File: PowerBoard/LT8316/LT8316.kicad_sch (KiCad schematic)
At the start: 42 parts, among them J1 AuxConn, Q1 STD11N65M2, SW1 POWER_SW, T1 11328-T078, U2 LT8316EFE#PBF

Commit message: nearlyready
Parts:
- C15: MPN (none) -> C2918513
- C25: MPN C2761574 -> C240475
- C26: MPN (none) -> C240475
- J1: MPN C157991 -> C161870
- SW1: MPN (none) -> C144394
- T1: MPN (none) -> C7423050

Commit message: fixeddimensions
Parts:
- removed C25, C26: 2200uF 200V, Capacitor_THT:CP_Radial_D30.0mm_P10.00mm_SnapIn, symbol Device:C_Polarized
- removed H1, H2, H3, H4: BATT-Hole, MountingHole:MountingHole_3.2mm_M3, symbol Mechanical:MountingHole_Pad
- added C25 (x3), C26 (x3): 330u 200V, Capacitor_THT:CP_Radial_D18.0mm_P7.50mm, symbol Device:C_Polarized
- C12: value 47p 100V -> 47p; footprint Capacitor_SMD:C_0603_1608Metric -> Capacitor_SMD:C_0805_2012Metric; MPN C527044 -> C14857
- C8: footprint Capacitor_SMD:C_0805_2012Metric -> Capacitor_SMD:C_1206_3216Metric; MPN C784084 -> C113894
- R10: value 121k -> 120k; MPN C2933296 -> C17436
- R11: value 4.99k -> 6.2k; MPN C17677 -> C17767
- R12: value 44.2k -> 56k; MPN C2960780 -> C17756
- R3: value 499k -> 470k; footprint Resistor_SMD:R_1206_3216Metric -> Resistor_SMD:R_0805_2012Metric; MPN C102210 -> C17709
- R7: value 56.2k -> 56k; MPN C2930117 -> C17756
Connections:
- net +BATT: now also C25.1, C25.1, C25.1, C26.1, C26.1, C26.1
- net -BATT: now also C25.2, C25.2, C25.2, C26.2, C26.2, C26.2
- no-connect marks 4 -> 0
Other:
- note added: "EN Voltage divider has to provide voltage > 1.2V but cannot exeed 40V 470k and 20k gives operating range 30-300V+ giving 1.224V and 12.24V"
- note added: "For 100x220 enclosure"
- note added: "Power supply for 200V applications"
- note added: "Total Capacity 1980uF"
- note added: "transformer replacements Sumida 11328-T074 - 12V/3A Würth 750317463 - 12V/4A Würth 750317589 - 12V/3A"
- note removed: "EN Voltage divider has to provide voltage > 1.2V but cannot exeed 40V 499k and 20k gives operating range 32-300V+ giving 1.233V and 11.5V"
- note removed: "Total Capacity 4400uF"
- moved on the sheet: C10, C11, C12, C13, C14, C15, C16, C17, C7, C8, C9, D1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

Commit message: small changes for lt
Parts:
- C10: value 47p 25V -> 47p; footprint Capacitor_SMD:C_0805_2012Metric -> GigaVescLibs:C_0603_1608Metric_L; MPN C14857 -> C1671
- C12: footprint Capacitor_SMD:C_0805_2012Metric -> GigaVescLibs:C_0603_1608Metric_L; MPN C14857 -> C1671
- C14: footprint Capacitor_SMD:C_0805_2012Metric -> Capacitor_SMD:C_0603_1608Metric; MPN C28260 -> C1604
- C9: footprint Capacitor_SMD:C_0805_2012Metric -> GigaVescLibs:C_0603_1608Metric_L; MPN C28233 -> C14663
- R1: footprint Resistor_SMD:R_0805_2012Metric -> Resistor_SMD:R_0603_1608Metric; MPN C149504 -> C25803
- R10: footprint Resistor_SMD:R_0805_2012Metric -> Resistor_SMD:R_0603_1608Metric; MPN C17436 -> C25808
- R11: footprint Resistor_SMD:R_0805_2012Metric -> Resistor_SMD:R_0603_1608Metric; MPN C17767 -> C4260
- R12: footprint Resistor_SMD:R_0805_2012Metric -> Resistor_SMD:R_0603_1608Metric; MPN C17756 -> C23206
- R13: footprint Resistor_SMD:R_0805_2012Metric -> Resistor_SMD:R_0603_1608Metric; MPN C17544 -> C22950
- R14: footprint Resistor_SMD:R_0805_2012Metric -> Resistor_SMD:R_0603_1608Metric; MPN C17408 -> C22775
- R16, R4: footprint Resistor_SMD:R_0805_2012Metric -> Resistor_SMD:R_0603_1608Metric; MPN C4328 -> C4184
- R2: footprint Resistor_SMD:R_0805_2012Metric -> Resistor_SMD:R_0603_1608Metric; MPN C17398 -> C4177
- R3: footprint Resistor_SMD:R_0805_2012Metric -> Resistor_SMD:R_0603_1608Metric; MPN C17709 -> C23178
- R6: footprint Resistor_SMD:R_0805_2012Metric -> Resistor_SMD:R_0603_1608Metric; MPN C17414 -> C25804
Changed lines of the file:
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@@
       (effects (font (size 1.27 1.27)))
     )
-    (property "Footprint" "Resistor_SMD:R_0805_2012Metric" (at 68.58 128.778 90)
+    (property "Footprint" "Resistor_SMD:R_0603_1608Metric" (at 68.58 128.778 90)
       (effects (font (size 1.27 1.27)) hide)
     )
@@
       (effects (font (size 1.27 1.27)) hide)
     )
-    (property "MPN" "C4328" (at 68.58 127 90)
+    (property "MPN" "C4184" (at 68.58 127 90)
       (effects (font (size 1.27 1.27)) hide)
     )
@@
       (effects (font (size 1.27 1.27)))
     )
-    (property "Footprint" "Resistor_SMD:R_0805_2012Metric" (at 153.67 140.208 90)
+    (property "Footprint" "Resistor_SMD:R_0603_1608Metric" (at 153.67 140.208 90)
       (effects (font (size 1.27 1.27)) hide)
     )
@@
       (effects (font (size 1.27 1.27)) hide)
     )
-    (property "MPN" "C17544" (at 153.67 138.43 90)
+    (property "MPN" "C22950" (at 153.67 138.43 90)
       (effects (font (size 1.27 1.27)) hide)
     )
@@
       (effects (font (size 1.27 1.27)))
     )
-    (property "Footprint" "Resistor_SMD:R_0805_2012Metric" (at 67.31 103.378 90)
+    (property "Footprint" "Resistor_SMD:R_0603_1608Metric" (at 67.31 103.378 90)
       (effects (font (size 1.27 1.27)) hide)
     )
@@
       (effects (font (size 1.27 1.27)) hide)
     )
-    (property "MPN" "C4328" (at 67.31 101.6 90)
+    (property "MPN" "C4184" (at 67.31 101.6 90)
       (effects (font (size 1.27 1.27)) hide)
     )
@@
       (effects (font (size 1.27 1.27)) (justify left))
     )
-    (property "Footprint" "Resistor_SMD:R_0805_2012Metric" (at 139.192 129.54 90)
+    (property "Footprint" "Resistor_SMD:R_0603_1608Metric" (at 139.192 129.54 90)
       (effects (font (size 1.27 1.27)) hide)
     )
@@
       (effects (font (size 1.27 1.27)) hide)
     )
-    (property "MPN" "C17767" (at 140.97 129.54 0)
+    (property "MPN" "C4260" (at 140.97 129.54 0)
       (effects (font (size 1.27 1.27)) hide)
     )
@@
       (effects (font (size 1.27 1.27)) (justify left))
     )
-    (property "Footprint" "Capacitor_SMD:C_0805_2012Metric" (at 59.3852 146.05 0)
+    (property "Footprint" "GigaVescLibs:C_0603_1608Metric_L" (at 59.3852 146.05 0)
       (effects (font (size 1.27 1.27)) hide)
     )
@@
       (effects (font (size 1.27 1.27)) hide)
     )
-    (property "MPN" "C28233" (at 58.42 142.24 0)
+    (property "MPN" "C14663" (at 58.42 142.24 0)
       (effects (font (size 1.27 1.27)) hide)
     )
@@
       (effects (font (size 1.27 1.27)) (justify left))
     )
-    (property "Footprint" "Resistor_SMD:R_0805_2012Metric" (at 200.152 63.5 90)
+    (property "Footprint" "Resistor_SMD:R_0603_1608Metric" (at 200.152 63.5 90)
       (effects (font (size 1.27 1.27)) hide)
     )
@@
       (effects (font (size 1.27 1.27)) hide)
     )
-    (property "MPN" "C149504" (at 201.93 63.5 0)
+    (property "MPN" "C25803" (at 201.93 63.5 0)
       (effects (font (size 1.27 1.27)) hide)
     )
@@
       (effects (font (size 1.27 1.27)) (justify left))
     )
-    (property "Footprint" "Resistor_SMD:R_0805_2012Metric" (at 139.192 121.92 90)
+    (property "Footprint" "Resistor_SMD:R_0603_1608Metric" (at 139.192 121.92 90)
       (effects (font (size 1.27 1.27)) hide)
     )
@@
       (effects (font (size 1.27 1.27)) hide)
     )
-    (property "MPN" "C17756" (at 140.97 121.92 0)
+    (property "MPN" "C23206" (at 140.97 121.92 0)
       (effects (font (size 1.27 1.27)) hide)
     )
@@
       (effects (font (size 1.27 1.27)) (justify left))
     )
-    (property "Footprint" "Resistor_SMD:R_0805_2012Metric" (at 200.152 78.74 90)
+    (property "Footprint" "Resistor_SMD:R_0603_1608Metric" (at 200.152 78.74 90)
       (effects (font (size 1.27 1.27)) hide)
     )
@@
       (effects (font (size 1.27 1.27)) hide)
     )
-    (property "MPN" "C17398" (at 201.93 78.74 0)
+    (property "MPN" "C4177" (at 201.93 78.74 0)
       (effects (font (size 1.27 1.27)) hide)
     )
@@
       (effects (font (size 1.27 1.27)) (justify left))
     )
-    (property "Footprint" "Resistor_SMD:R_0805_2012Metric" (at 70.612 95.25 90)
+    (property "Footprint" "Resistor_SMD:R_0603_1608Metric" (at 70.612 95.25 90)
       (effects (font (size 1.27 1.27)) hide)
     )
@@
       (effects (font (size 1.27 1.27)) hide)
     )
-    (property "MPN" "C17709" (at 72.39 95.25 0)
+    (property "MPN" "C23178" (at 72.39 95.25 0)
       (effects (font (size 1.27 1.27)) hide)
     )
@@
       (effects (font (size 1.27 1.27)) (justify left))
     )
-    (property "Footprint" "Capacitor_SMD:C_0805_2012Metric" (at 124.1552 105.41 0)
+    (property "Footprint" "GigaVescLibs:C_0603_1608Metric_L" (at 124.1552 105.41 0)
       (effects (font (size 1.27 1.27)) hide)
     )
@@
       (effects (font (size 1.27 1.27)) hide)
     )
-    (property "MPN" "C14857" (at 123.19 101.6 0)
+    (property "MPN" "C1671" (at 123.19 101.6 0)
       (effects (font (size 1.27 1.27)) hide)
     )
@@
       (effects (font (size 1.27 1.27)) (justify left))
     )
-    (property "Footprint" "Resistor_SMD:R_0805_2012Metric" (at 56.642 134.62 90)
+    (property "Footprint" "Resistor_SMD:R_0603_1608Metric" (at 56.642 134.62 90)
       (effects (font (size 1.27 1.27)) hide)
     )
@@
       (effects (font (size 1.27 1.27)) hide)
     )
-    (property "MPN" "C17414" (at 58.42 134.62 0)
+    (property "MPN" "C25804" (at 58.42 134.62 0)
       (effects (font (size 1.27 1.27)) hide)
     )
@@
       (effects (font (size 1.27 1.27)) (justify left))
     )
-    (property "Footprint" "Resistor_SMD:R_0805_2012Metric" (at 129.032 129.54 90)
+    (property "Footprint" "Resistor_SMD:R_0603_1608Metric" (at 129.032 129.54 90)
       (effects (font (size 1.27 1.27)) hide)
     )
@@
       (effects (font (size 1.27 1.27)) hide)
     )
-    (property "MPN" "C17436" (at 130.81 129.54 0)
+    (property "MPN" "C25808" (at 130.81 129.54 0)
       (effects (font (size 1.27 1.27)) hide)
     )
@@
       (effects (font (size 1.27 1.27)) (justify left))
     )
-    (property "Value" "47p 25V" (at 36.83 140.97 0)
-      (effects (font (size 1.27 1.27)) (justify left))
-    )
-    (property "Footprint" "Capacitor_SMD:C_0805_2012Metric" (at 46.6852 142.24 0)
+    (property "Value" "47p" (at 36.83 140.97 0)
+      (effects (font (size 1.27 1.27)) (justify left))
+    )
+    (property "Footprint" "GigaVescLibs:C_0603_1608Metric_L" (at 46.6852 142.24 0)
       (effects (font (size 1.27 1.27)) hide)
     )
@@
       (effects (font (size 1.27 1.27)) hide)
     )
-    (property "MPN" "C14857" (at 45.72 138.43 0)
+    (property "MPN" "C1671" (at 45.72 138.43 0)
       (effects (font (size 1.27 1.27)) hide)
     )
@@
       (effects (font (size 1.27 1.27)) (justify left))
     )
-    (property "Footprint" "Capacitor_SMD:C_0805_2012Metric" (at 190.5 148.8948 0)
+    (property "Footprint" "Capacitor_SMD:C_0603_1608Metric" (at 190.5 148.8948 0)
       (effects (font (size 1.27 1.27)) hide)
     )
@@
       (effects (font (size 1.27 1.27)) hide)
     )
-    (property "MPN" "C28260" (at 186.69 149.86 0)
+    (property "MPN" "C1604" (at 186.69 149.86 0)
       (effects (font (size 1.27 1.27)) hide)
     )
@@
       (effects (font (size 1.27 1.27)))
     )
-    (property "Footprint" "Resistor_SMD:R_0805_2012Metric" (at 153.67 144.018 90)
+    (property "Footprint" "Resistor_SMD:R_0603_1608Metric" (at 153.67 144.018 90)
       (effects (font (size 1.27 1.27)) hide)
     )
@@
       (effects (font (size 1.27 1.27)) hide)
     )
-    (property "MPN" "C17408" (at 153.67 142.24 90)
-      (effects (font (size 1.27 1.27)) hide)
-    )
+    (property "MPN" "C22775" (at 153.67 142.24 90)
+      (effects (font (size 1.27 1.27)) hide)
+    )

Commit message: fix
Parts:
- R1: value 100k -> 150k; MPN C25803 -> C22807
- R2: value 1.8k -> 2.7k; MPN C4177 -> C13167
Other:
- note added: "Division up to 186V => 3.3V !!Those values have to be the same as on mosfet board!!"
- note removed: "Voltage divider 188V = 3.3V"
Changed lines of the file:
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@@
     (effects (font (size 1.27 1.27)) (justify left bottom))
   )
-  (text "Voltage divider\n188V = 3.3V" (at 181.61 72.39 0)
+  (text "Division up to 186V => 3.3V\n!!Those values have to be the same as on mosfet board!!"
+    (at 170.18 54.61 0)
     (effects (font (size 1.27 1.27)) (justify left bottom))
   )
@@
       (effects (font (size 1.27 1.27)) (justify left))
     )
-    (property "Value" "100k" (at 204.47 64.77 0)
+    (property "Value" "150k" (at 204.47 64.77 0)
       (effects (font (size 1.27 1.27)) (justify left))
     )
@@
       (effects (font (size 1.27 1.27)) hide)
     )
-    (property "MPN" "C25803" (at 201.93 63.5 0)
+    (property "MPN" "C22807" (at 201.93 63.5 0)
       (effects (font (size 1.27 1.27)) hide)
     )
@@
       (effects (font (size 1.27 1.27)) (justify left))
     )
-    (property "Value" "1.8k" (at 204.47 80.01 0)
+    (property "Value" "2.7k" (at 204.47 80.01 0)
       (effects (font (size 1.27 1.27)) (justify left))
     )
@@
       (effects (font (size 1.27 1.27)) hide)
     )
-    (property "MPN" "C4177" (at 201.93 78.74 0)
-      (effects (font (size 1.27 1.27)) hide)
-    )
+    (property "MPN" "C13167" (at 201.93 78.74 0)
+      (effects (font (size 1.27 1.27)) hide)
+    )

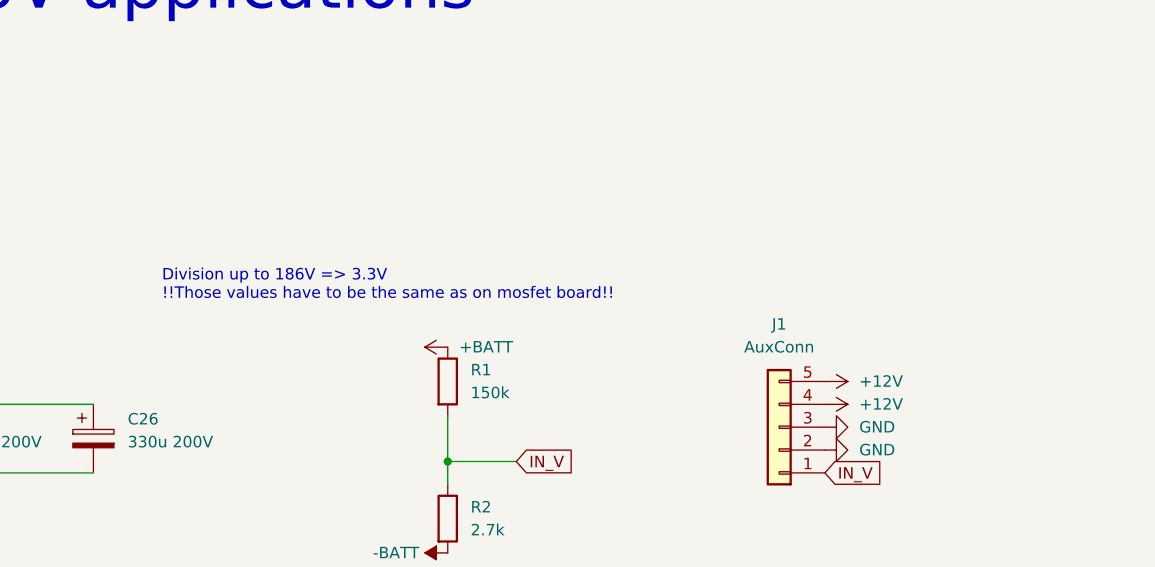
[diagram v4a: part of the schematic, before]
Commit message: v3.0.0 - GaN redesign begin
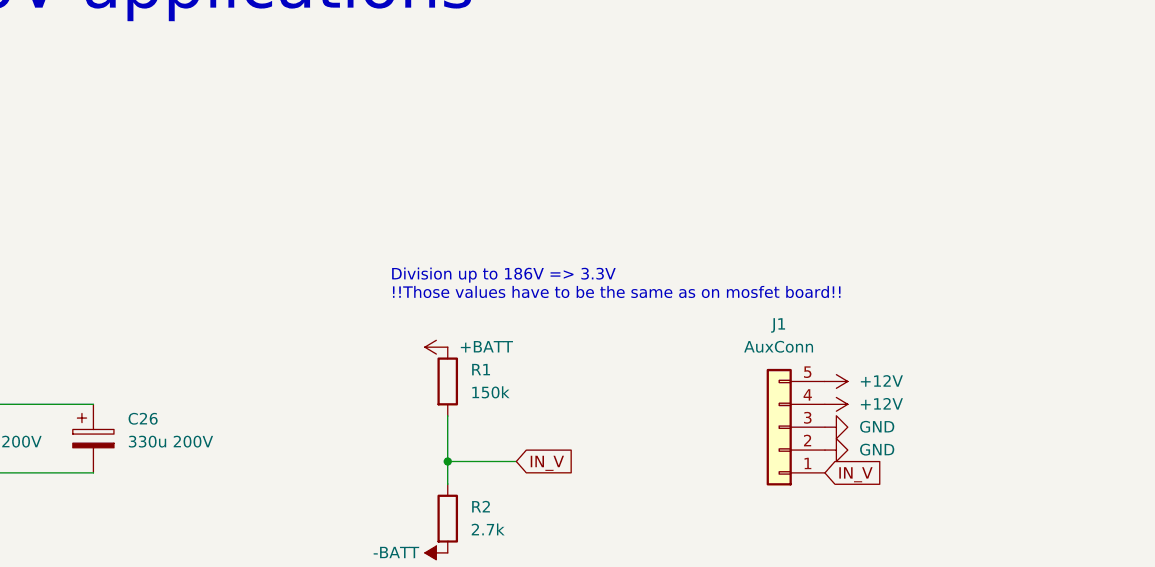
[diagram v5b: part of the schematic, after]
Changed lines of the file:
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@@
   )
   (text "Division up to 186V => 3.3V\n!!Those values have to be the same as on mosfet board!!"
-    (at 170.18 54.61 0)
+    (at 195.58 54.61 0)
     (effects (font (size 1.27 1.27)) (justify left bottom))
   )
